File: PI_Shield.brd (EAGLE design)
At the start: 80.1 x 86.7 mm, 67 parts, among them Q1 220mA/50V/3.5Ω, Q3 220mA/50V/3.5Ω, Q4 220mA/50V/3.5Ω, Q5 2.5A/30V/105mΩ, U1 MAX1136EUA-T, U2 AZ1117EH-3.3TRG1, Y1 ECS-80-S-4X

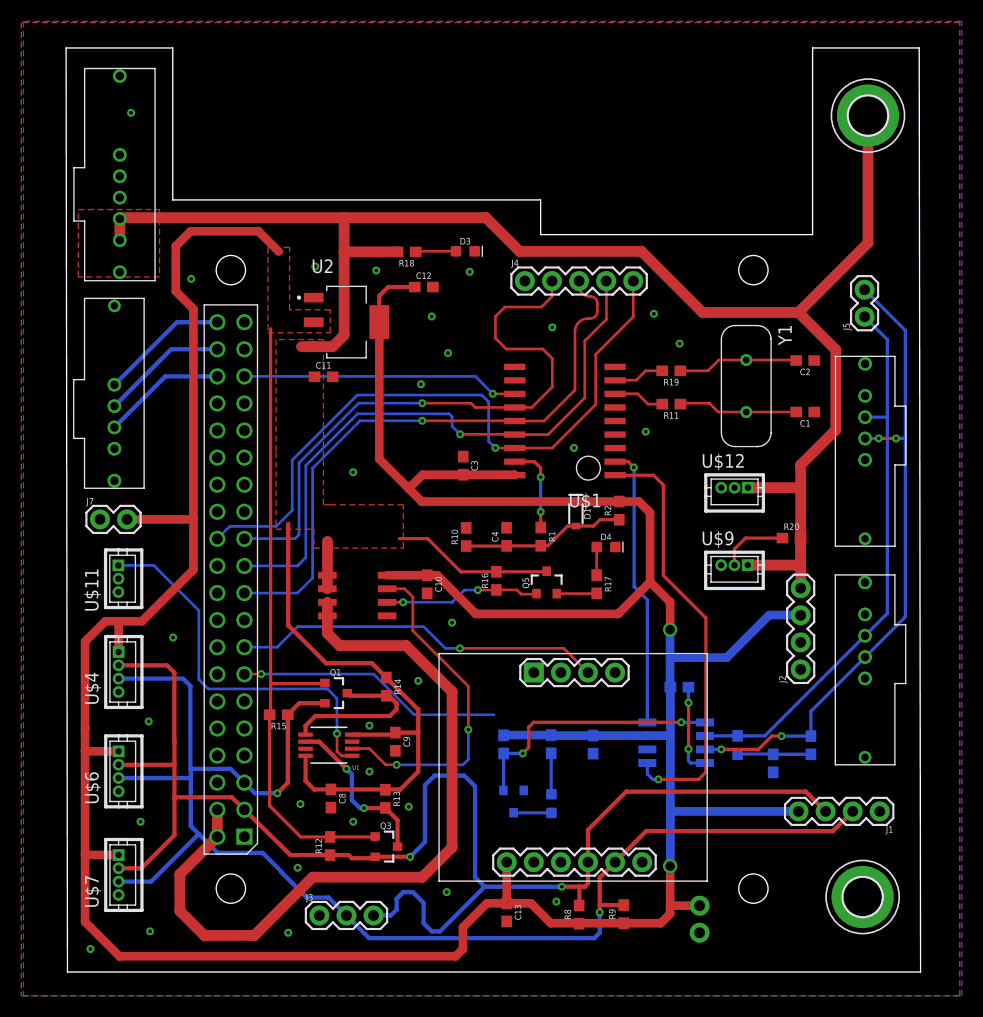
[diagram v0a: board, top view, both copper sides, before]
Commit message: Most of Changes done, need to impedance match
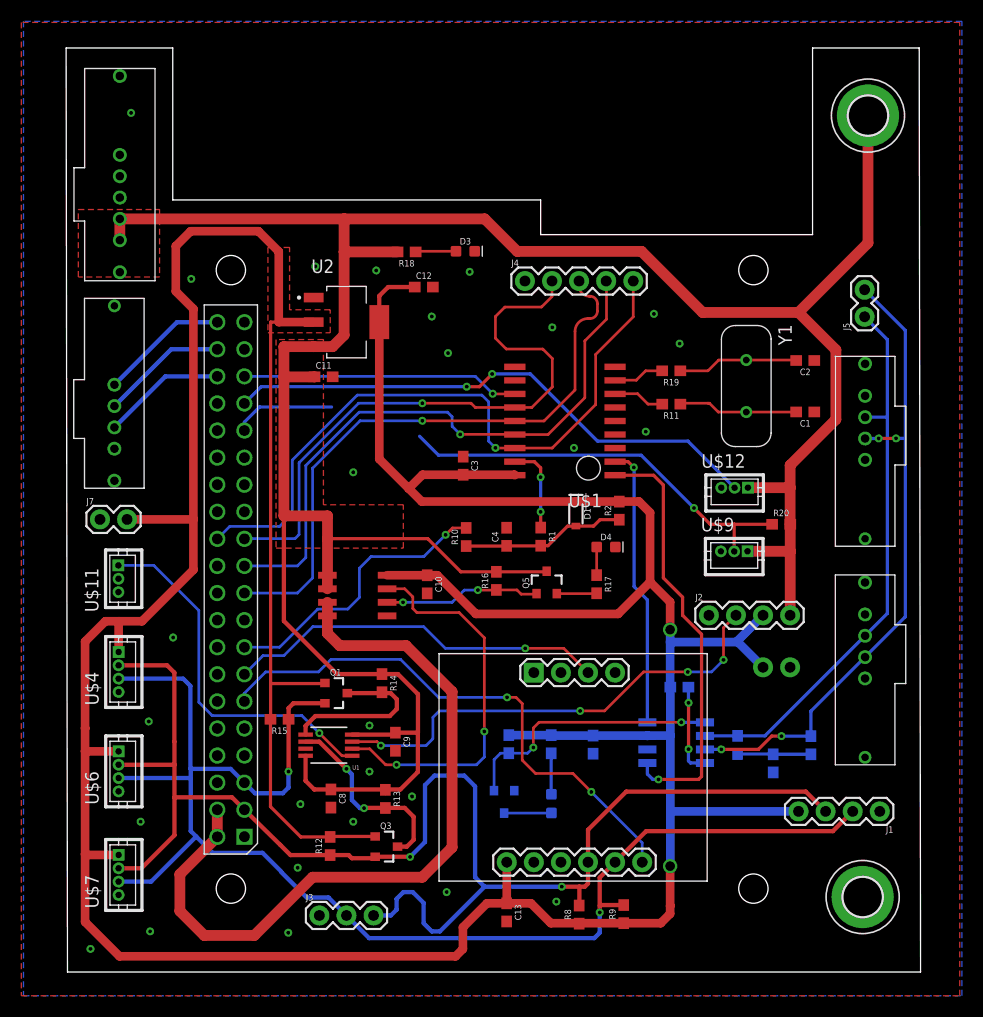
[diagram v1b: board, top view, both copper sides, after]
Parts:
- moved J6 26.3 mm to (67.9, 26.9), turned to 0 degrees
- moved J2 10.00 mm to (60.3, 31.8), turned to 0 degrees
- moved R20 1.62 mm to (67.1, 40.3)
- moved U$9 1.30 mm to (62.7, 37.8)
- moved Q4 0.89 mm to (41.1, 14.4)
- moved R14 0.52 mm to (29.6, 25.4)
- moved R4 0.48 mm to (41.5, 19.7)
- moved R15 0.44 mm to (20.0, 22.0)
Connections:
- net DI: now also PCB1.P$31
- net IMU_INT: now also PCB1.P$13; no longer PCB1.P$15
- net IMU_RESET: now also PCB1.P$11; no longer PCB1.P$13
- net PWM: now also PCB1.P$33; no longer PCB1.P$32
- net RESET_TO_PI: now also PCB1.P$15
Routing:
- net PWM: track 0.00 -> 51.5 mm, vias 0 -> 2
- net AIN2: track 0.00 -> 44.1 mm, vias 0 -> 4
- net DI: track 6.43 -> 48.6 mm, vias 0 -> 1
- net 5V: track 220.1 -> 256.5 mm
- net RESET_TO_PI: track 0.00 -> 27.0 mm, vias 0 -> 1
- net IMU_RESET: track 25.0 -> 51.4 mm, vias 1 -> 2
- net 3V3: track 389.7 -> 397.0 mm
- net AMP_OUT: track 31.9 -> 36.2 mm
- net SDA_ADC: track 15.6 -> 18.4 mm
- net AIN: track 36.0 -> 34.4 mm
- net IMU_INT: track 34.8 -> 35.9 mm
- net N$4: track 3.56 -> 4.44 mm
- net SCL: track 133.8 -> 134.4 mm
- net FAULT: track 24.7 -> 25.2 mm

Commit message: Changes done
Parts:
- moved J7 1.02 mm to (4.19, 40.8)
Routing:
- net 5V: track 256.5 -> 294.0 mm
- net RXCAN: track 26.4 -> 38.6 mm
- net DI: track 48.6 -> 57.2 mm, vias 1 -> 3
- net CANL: track 52.7 -> 60.2 mm
- net SDA: track 137.1 -> 133.9 mm
- net AMP_OUT: track 36.2 -> 34.1 mm
- net SCL_ADC: track 15.9 -> 17.9 mm
- net 3V3: track 397.0 -> 395.7 mm
- net CLK: track 57.4 -> 56.7 mm
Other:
- outline, holes or cut-outs redrawn

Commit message: More Changes
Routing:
- net TXCAN: track 40.5 -> 32.1 mm, vias 1 -> 3
- net RXCAN: track 38.6 -> 31.6 mm
- net CS: track 63.0 -> 65.8 mm, vias 1 -> 3
- net CLK: track 56.7 -> 54.4 mm
- net FAULT: track 25.2 -> 25.7 mm

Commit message: Even more changes
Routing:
- net CANL: track 60.2 -> 53.3 mm
- net CANH: track 61.3 -> 58.7 mm, vias 4 -> 2
- net CLK: track 54.4 -> 55.1 mm

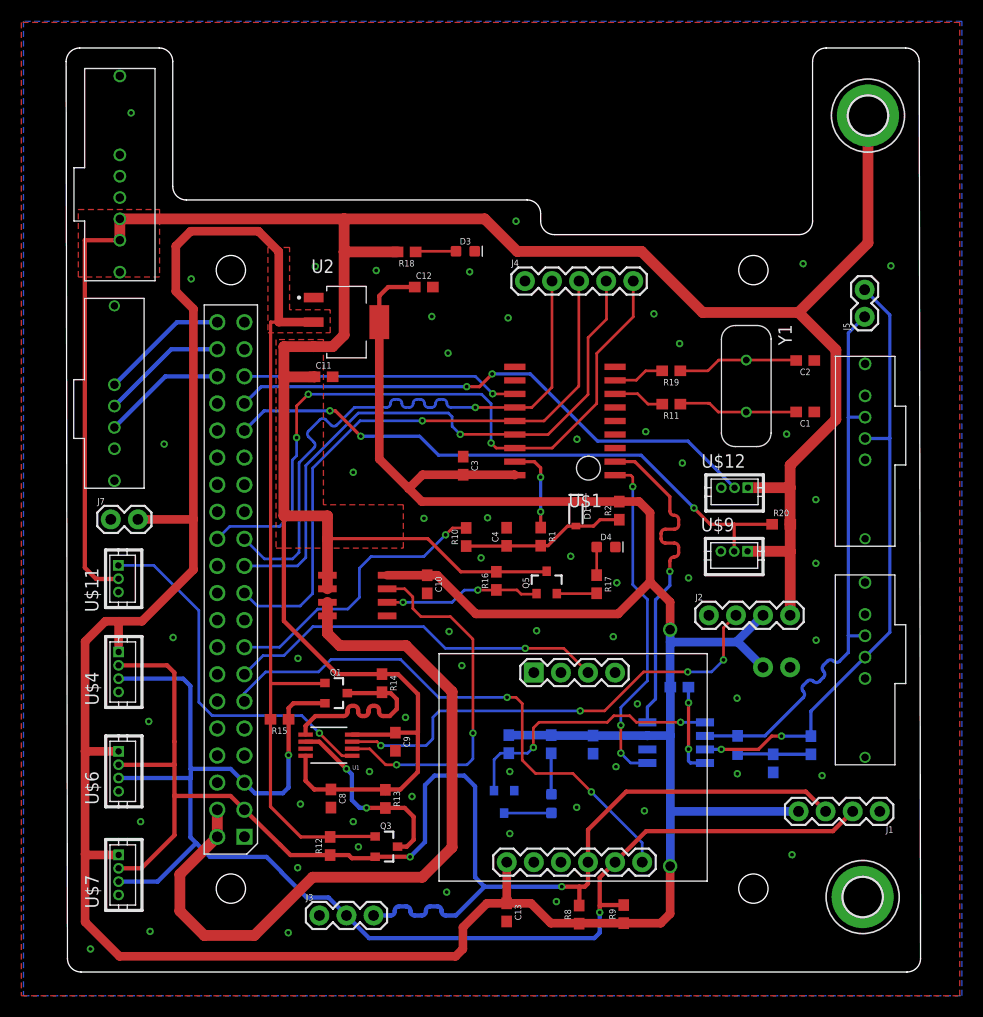
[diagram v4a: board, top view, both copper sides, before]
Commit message: Added Silkscreen Text
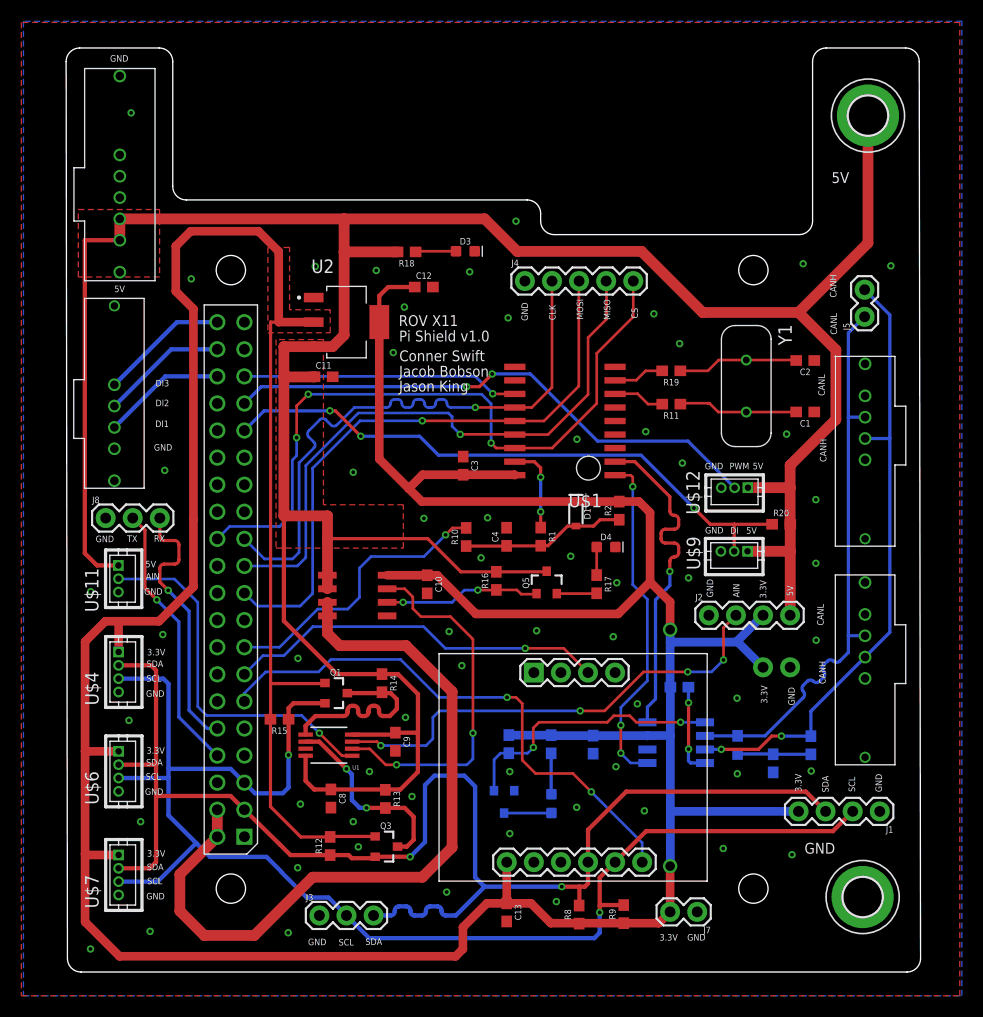
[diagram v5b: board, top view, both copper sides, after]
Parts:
- added J8: (no value), SparkFun-Connectors:1X03
- moved J7 66.2 mm to (59.2, 3.99), turned to 180 degrees
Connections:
- new net RX: J8.3, PCB1.P$10
- new net TX: J8.2, PCB1.P$8
- net 5V: now also U$11.P$1; no longer U$11.P$2
- net AIN: now also U$11.P$2; no longer U$11.P$1
- net GND: now also J8.1
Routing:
- net TX: track 0.00 -> 25.6 mm, vias 0 -> 1
- net RX: track 0.00 -> 25.1 mm, vias 0 -> 1
- net 3V3: track 395.7 -> 391.3 mm
- net SDA: track 133.9 -> 132.1 mm
- net 5V: track 294.0 -> 292.6 mm
- net SCL: track 134.5 -> 133.3 mm
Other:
- board text added: "3.3V"
- board text added: "5V"
- board text added: "AIN"
- board text added: "CANH"
- board text added: "CANL"
- board text added: "CLK"
- board text added: "CS"
- board text added: "Conner Swift"
- board text added: "DI"
- board text added: "DI1"
- board text added: "DI2"
- board text added: "DI3"
- board text added: "GND"
- board text added: "Jacob Bobson"
- board text added: "Jason King"
- board text added: "MISO"
- board text added: "MOSI"
- board text added: "PWM"
- board text added: "Pi Shield v1.0"
- board text added: "ROV X11"
- board text added: "RX"
- board text added: "SCL"
- board text added: "SDA"
- board text added: "TX"
